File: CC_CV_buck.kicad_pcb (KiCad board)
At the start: 4 copper layers, 115.9 x 39 mm, 76 parts, among them J5 Conn_01x02_Pin, J6 Conn_01x02_Pin, J7 Conn_01x02_Pin, J8 Conn_01x02_Pin, Q1 TIP42C, Q2 AO3400A, Q3 MMBT3906, U1 OPA2197xD, U2 INA194, U3 AOZ6605PI-1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

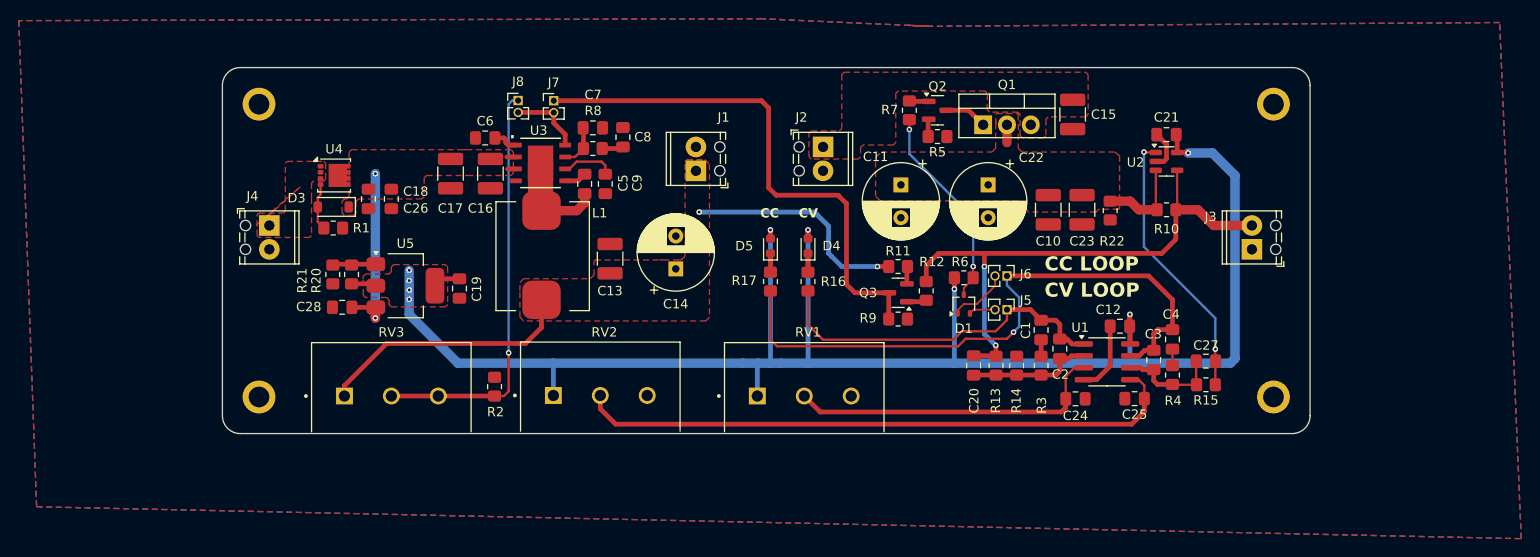
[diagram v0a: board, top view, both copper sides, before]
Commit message: add series resistor to potentiometers to limit maximum setpoint voltages
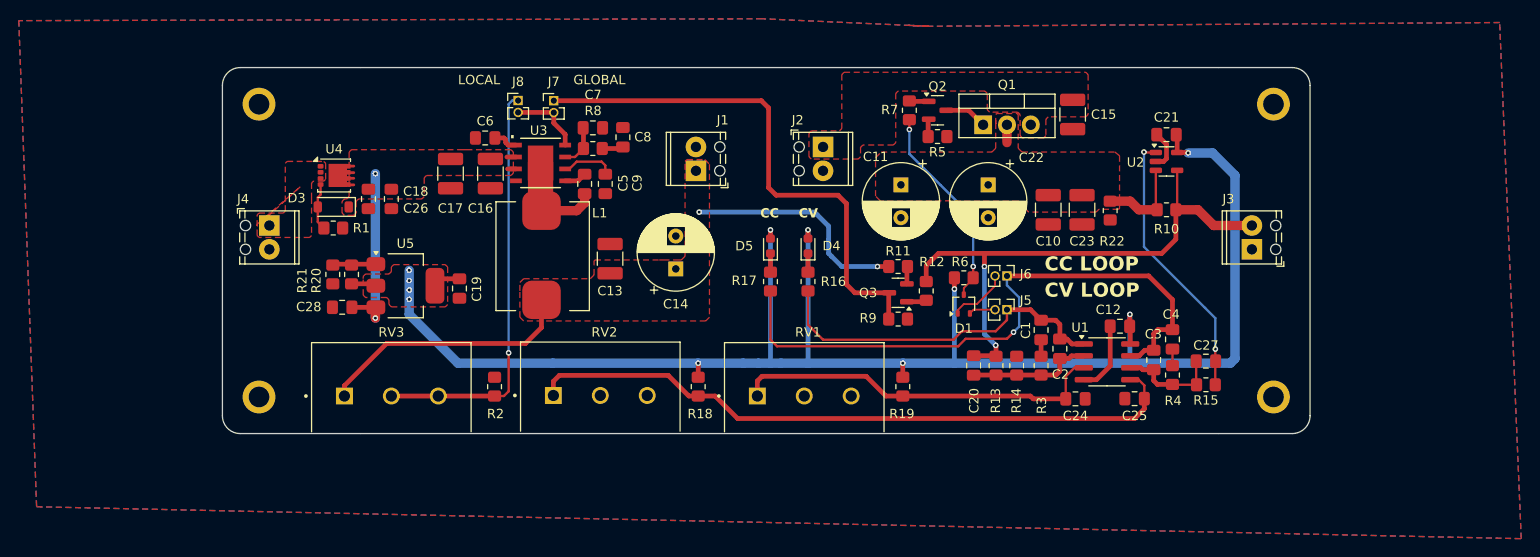
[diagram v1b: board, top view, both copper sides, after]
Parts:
- added R18: 60k, Resistor_SMD:R_0805_2012Metric_Pad1.20x1.40mm_HandSolder, F.Cu at (101.7, 103.0)
- added R19: 20k, Resistor_SMD:R_0805_2012Metric_Pad1.20x1.40mm_HandSolder, F.Cu at (123.5, 103.0)
- R7: value 1 -> 0
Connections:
- RV1 pad 1: Vcc -> /VSET
- RV1 pad 2: /VSET -> GND
- RV2 pad 1: Vcc -> /ISET
- RV2 pad 2: /ISET -> GND
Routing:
- net /VSET: track 34.4 -> 40.8 mm
- net /ISET: track 65.2 -> 71.3 mm
- net Vcc: track 184.0 -> 180.0 mm, vias 9 -> 11
- net VIN_P: track 21.7 -> 24.9 mm
- added copper zone on In2.Cu, net GND
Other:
- board text added: "GLOBAL"
- board text added: "LOCAL"

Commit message: add some stitching
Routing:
- net GND: vias 0 -> 180
